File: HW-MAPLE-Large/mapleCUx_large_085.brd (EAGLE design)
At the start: 100 x 59 mm, 56 parts, among them IC1 DS2482, IC2 LAN-USR-ES1, Q1 BSS84, X4 1751248, X7 1751264

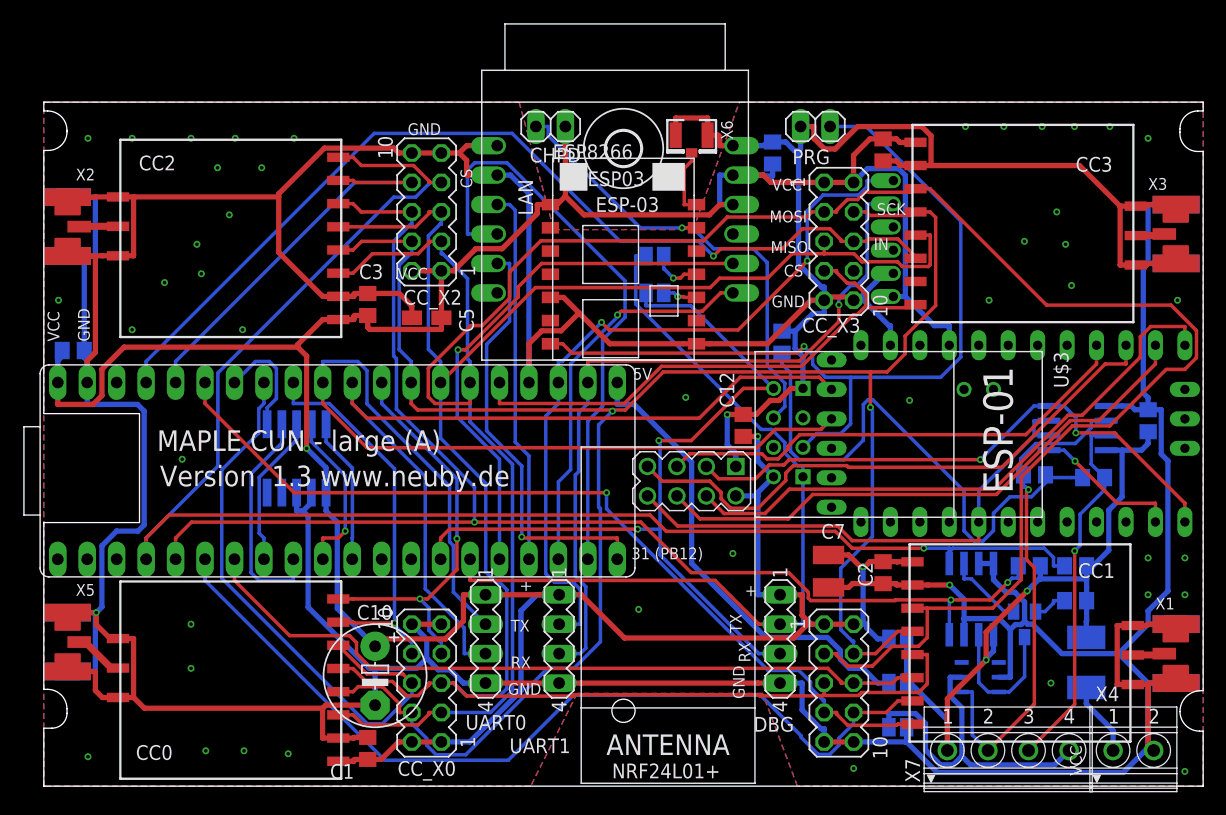
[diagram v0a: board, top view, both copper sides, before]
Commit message: Small Fixes + other RX+TX Pins at Arduino
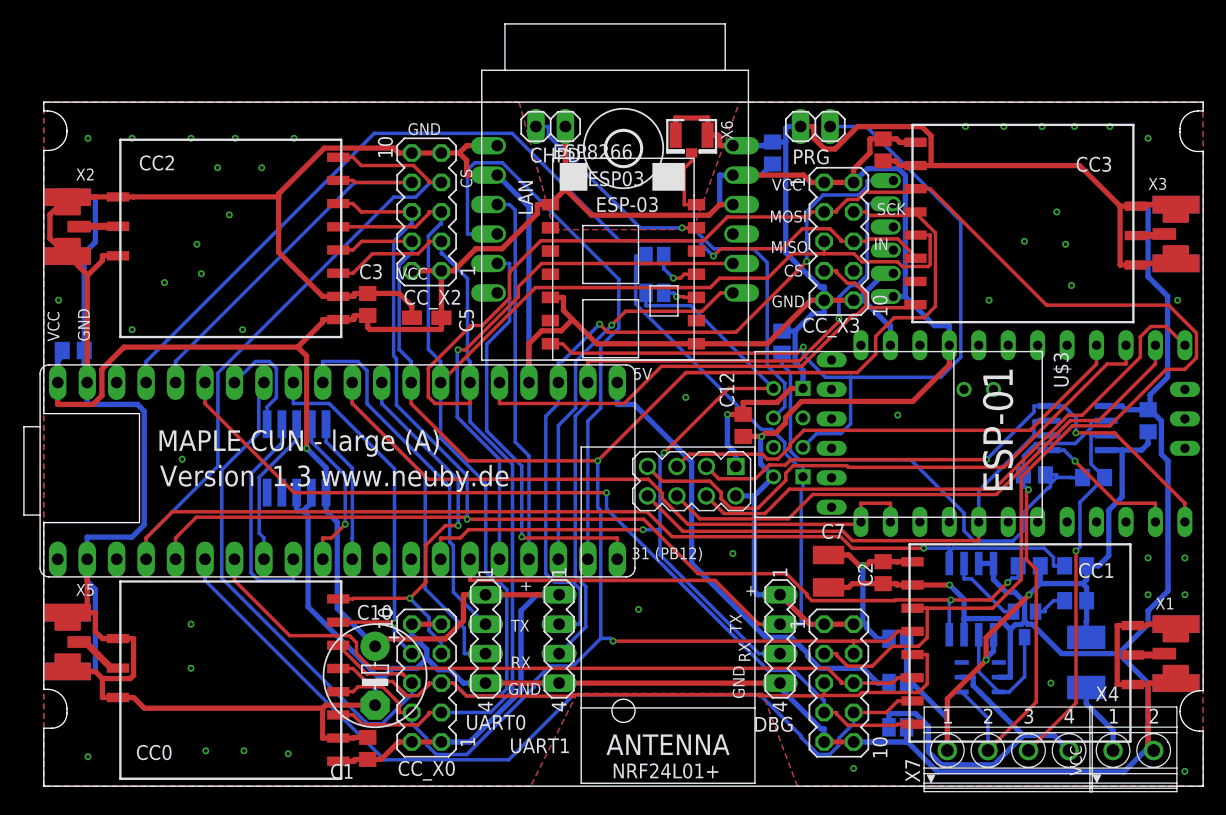
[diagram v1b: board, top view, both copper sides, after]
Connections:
- net GND: now also U$1.2
- net RX-MAPLE: now also U$2.RX1, U$2.TX0; no longer U$2.TX0-1
- net TX-MAPLE: no longer U$2.RX1-1
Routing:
- net TX-MAPLE: track 80.4 -> 32.1 mm
- net RX-MAPLE: track 74.8 -> 85.3 mm
- net N$21: track 48.9 -> 42.6 mm
- net GND: track 601.7 -> 607.4 mm, vias 3 -> 2
- net SCK1: track 170.2 -> 164.6 mm
- net VCC: track 283.7 -> 279.3 mm
- net IRQ-A: track 45.1 -> 46.4 mm
- net RX1: track 64.9 -> 63.8 mm
- net RX_DBG: track 71.7 -> 70.7 mm
- net CSN-A: track 51.2 -> 50.3 mm
- net 1W: track 43.3 -> 42.6 mm
- net SCK2: track 51.5 -> 50.8 mm
- net N$48: track 12.4 -> 11.8 mm
